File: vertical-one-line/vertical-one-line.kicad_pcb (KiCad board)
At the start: 2 copper layers, 8.1 x 10.2 mm, 2 parts, among them J1 Grove-I2C-connector, J2 Conn_01x04

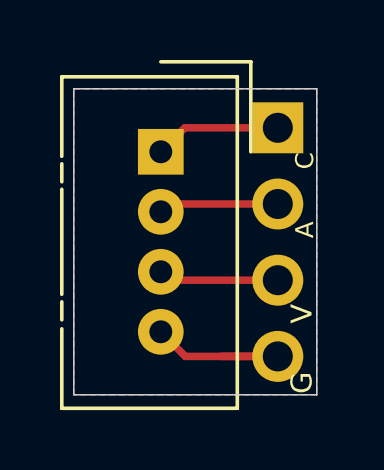
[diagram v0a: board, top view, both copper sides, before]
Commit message: Update silk lines for rev2021.02
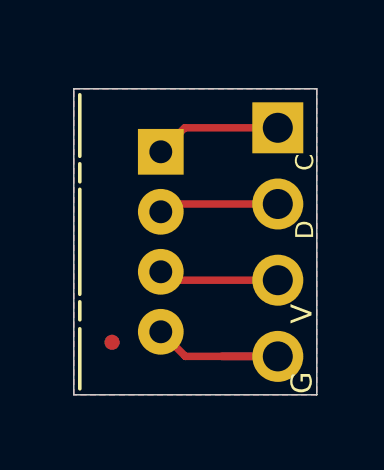
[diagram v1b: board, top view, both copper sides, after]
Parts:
- added fid1: Fiducial_0.5mm_Mask1mm, Fiducial:Fiducial_0.5mm_Mask1mm, B.Cu at (141.8, 108.8)
- added fid1: Fiducial_0.5mm_Mask1mm, Fiducial:Fiducial_0.5mm_Mask1mm, F.Cu at (141.8, 108.8)
- J1: footprint Connector:NS-Tech_Grove_1x04_P2mm_Vertical -> my-kicad-footprints:NS-Tech_Grove_1x04_P2mm_Vertical_silk_inside
- J2: footprint Connector_PinSocket_2.54mm:PinSocket_1x04_P2.54mm_Vertical -> my-kicad-footprints:PinHeader_1x04_P2.54mm_Vertical_silk_inside
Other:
- board text added: "D"
- board text added: "Rev2021.02"
- board text removed: "A"
- board text removed: "Rev2020.12"

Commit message: Update revision for bertical botn and one line and horizontal both
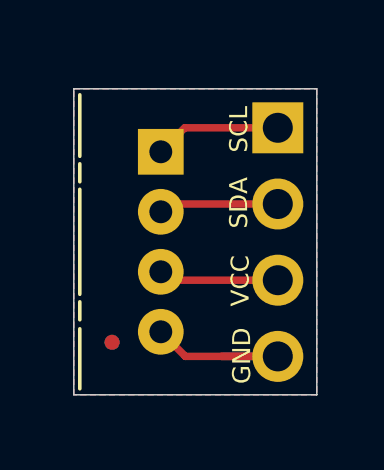
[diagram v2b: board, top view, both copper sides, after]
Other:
- board text added: "GND"
- board text added: "Rev2021.04"
- board text added: "SCL"
- board text added: "SDA"
- board text added: "VCC"
- board text removed: "C"
- board text removed: "D"
- board text removed: "G"
- board text removed: "Rev2021.02"
- board text removed: "V"
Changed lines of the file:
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@@
       (effects (font (size 1 1) (thickness 0.15)))
     )
+    (fp_circle (center 0 0) (end 0.5 0) (layer F.Fab) (width 0.1))
+    (fp_circle (center 0 0) (end 0.75 0) (layer F.CrtYd) (width 0.05))
     (fp_text user %R (at 0 0) (layer F.Fab)
       (effects (font (size 0.2 0.2) (thickness 0.04)))
     )
-    (fp_circle (center 0 0) (end 0.5 0) (layer F.Fab) (width 0.1))
-    (fp_circle (center 0 0) (end 0.75 0) (layer F.CrtYd) (width 0.05))
     (pad "" smd circle (at 0 0) (size 0.5 0.5) (layers F.Cu F.Mask)
       (solder_mask_margin 0.25) (clearance 0.25))
@@
     (arrow2b (pts (xy 150.3 110.5) (xy 149.713579 109.373496)))
   )
-  (gr_text Rev2021.02 (at 145.9 110) (layer B.SilkS)
+  (gr_text Rev2021.04 (at 145.9 110) (layer B.SilkS)
     (effects (font (size 0.6 0.6) (thickness 0.15)) (justify left mirror))
   )
@@
     (effects (font (size 0.6 0.6) (thickness 0.15)) (justify left mirror))
   )
-  (gr_text G (at 148.1 110.1 90) (layer F.SilkS)
-    (effects (font (size 0.7 0.7) (thickness 0.15)))
-  )
-  (gr_text C (at 148.2 102.75 90) (layer F.SilkS)
+  (gr_text GND (at 146.1 109.2 90) (layer F.SilkS)
     (effects (font (size 0.6 0.6) (thickness 0.15)))
   )
-  (gr_text V (at 148.1 107.8 90) (layer F.SilkS)
-    (effects (font (size 0.7 0.7) (thickness 0.15)))
+  (gr_text SCL (at 146 101.65 90) (layer F.SilkS)
+    (effects (font (size 0.6 0.6) (thickness 0.15)))
   )
-  (gr_text D (at 148.2 105 90) (layer F.SilkS)
+  (gr_text VCC (at 146.05 106.7 90) (layer F.SilkS)
+    (effects (font (size 0.6 0.6) (thickness 0.15)))
+  )
+  (gr_text SDA (at 146 104.1 90) (layer F.SilkS)
     (effects (font (size 0.6 0.6) (thickness 0.15)))
   )
@@
   (gr_line (start 140.5 110.5) (end 140.5 100.3) (layer Edge.Cuts) (width 0.05))
   (gr_line (start 148.6 110.5) (end 140.5 110.5) (layer Edge.Cuts) (width 0.05))
-  (segment (start 144.22 109.22) (end 143.4 108.4) (width 0.25) (layer F.Cu) (net 1))
-  (segment (start 147.3 109.22) (end 144.22 109.22) (width 0.25) (layer F.Cu) (net 1))
   (segment (start 147.3 109.22) (end 145.42 109.22) (width 0.25) (layer F.Cu) (net 1))
   (segment (start 147.3 109.22) (end 145.48 109.22) (width 0.25) (layer B.Cu) (net 1))
+  (segment (start 147.3 109.22) (end 144.22 109.22) (width 0.25) (layer F.Cu) (net 1))
+  (segment (start 144.22 109.22) (end 143.4 108.4) (width 0.25) (layer F.Cu) (net 1))
   (segment (start 143.68 106.68) (end 143.4 106.4) (width 0.25) (layer F.Cu) (net 2))
   (segment (start 147.3 106.68) (end 143.68 106.68) (width 0.25) (layer F.Cu) (net 2))
   (segment (start 143.66 104.14) (end 143.4 104.4) (width 0.25) (layer F.Cu) (net 3))
   (segment (start 147.3 104.14) (end 143.66 104.14) (width 0.25) (layer F.Cu) (net 3))
+  (segment (start 147.3 101.6) (end 144.2 101.6) (width 0.25) (layer F.Cu) (net 4))
   (segment (start 144.2 101.6) (end 143.4 102.4) (width 0.25) (layer F.Cu) (net 4))
-  (segment (start 147.3 101.6) (end 144.2 101.6) (width 0.25) (layer F.Cu) (net 4))
   (zone (net 1) (net_name GND) (layer F.Cu) (hatch edge 0.508)
     (connect_pads (clearance 0.508))
